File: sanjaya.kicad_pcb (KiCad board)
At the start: 2 copper layers, 72 parts, among them J1 PWR_SUPPLY, J10 Battery_Backup_Bypass, J11 USB_B_Micro_OUT, J12 ON_Switch, J13 Raspberry_Pi_2_3, J14 Fan, J15 Serial, J2 Digital_Input_Signals, J3 Digital_Gnd, J4 Screw_Terminal_01x03, J5 Screw_Terminal_01x03, J6 Screw_Terminal_01x02, J7 Screw_Terminal_01x02, J8 Supply_Safety_Bypass, J9 USB_B_Micro_IN, K1 Songle-SRD, K2 Songle-SRD, Q1 Q_PMOS_GSD, Q2 FDC021N30, SW2 SW_DIP_x04, U1 74HC14, U2 MCP9700T-ETT, U3 TPS2400BVR, U4 ULN2803A, U5 MCP3428, U6 TLP291-4, U7 MAX232, U8 SN65LBC176D

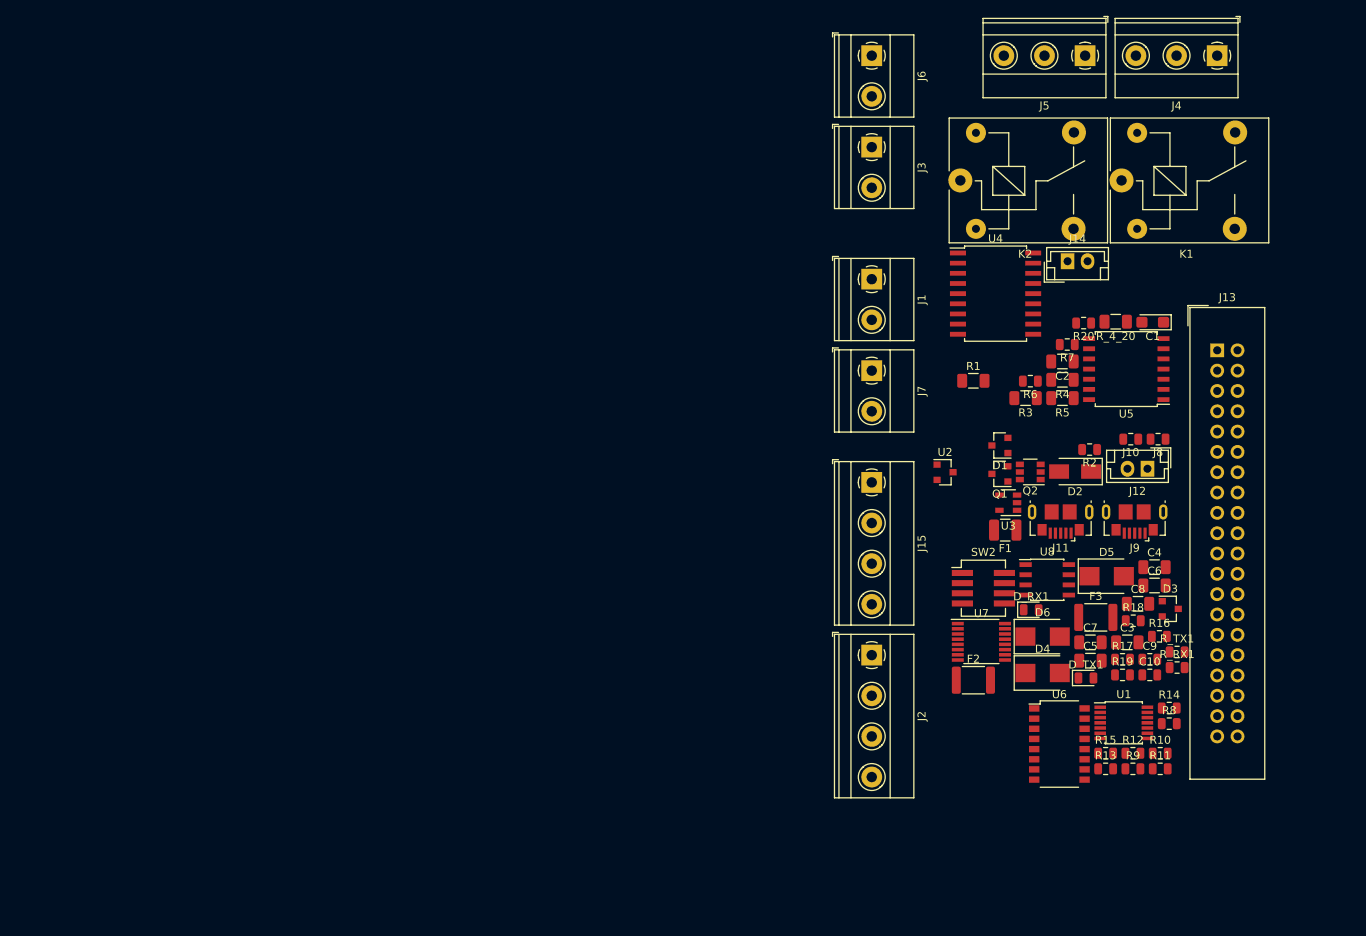
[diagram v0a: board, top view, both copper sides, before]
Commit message: Changes: 1. Removed TVS diodes in favour of a RS485 transceiver of the same footprint that contains ESD protection 2. Tried different layouts.
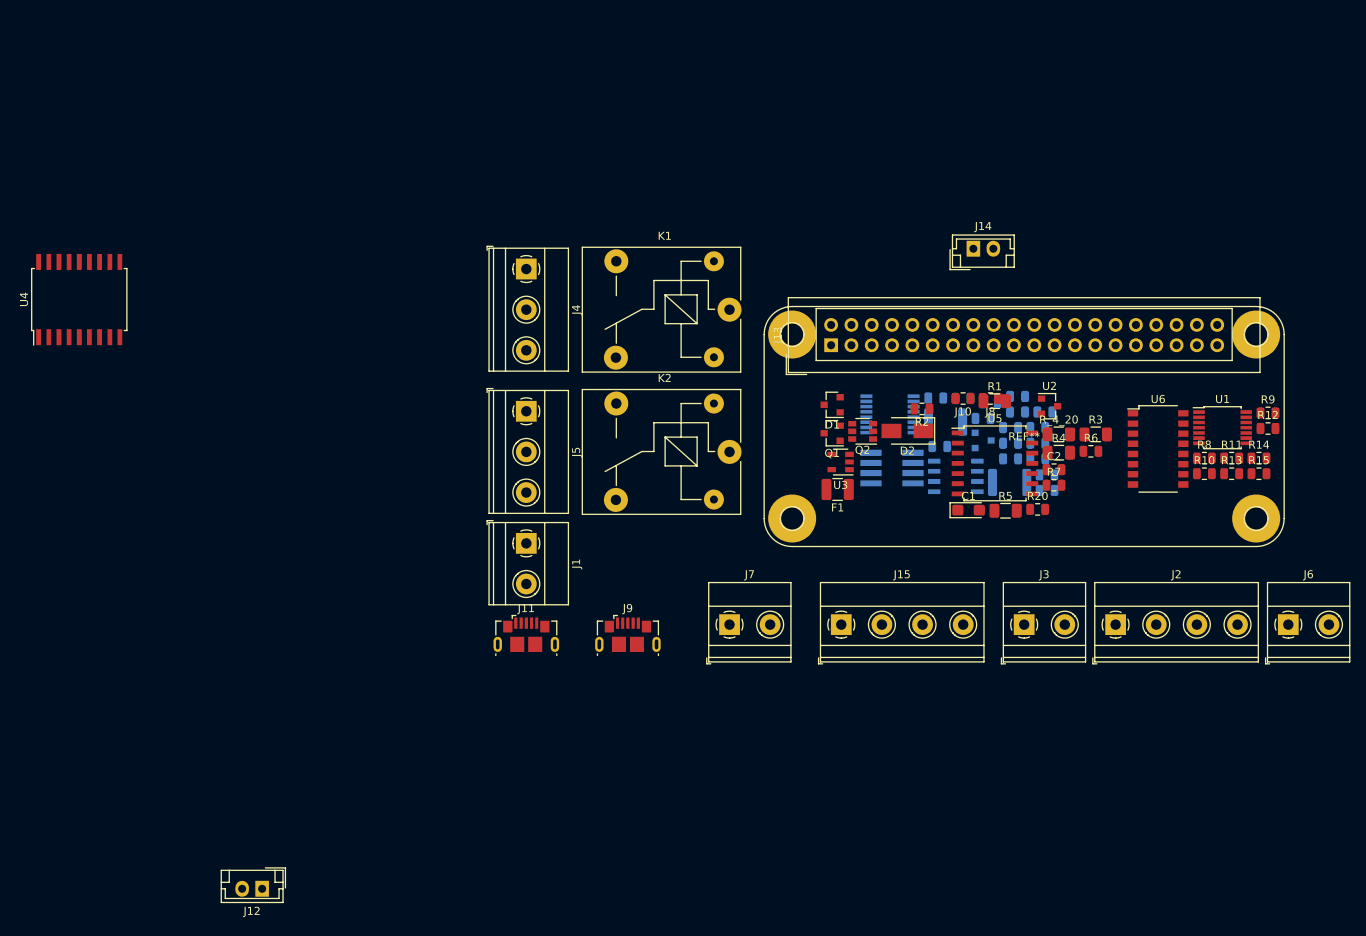
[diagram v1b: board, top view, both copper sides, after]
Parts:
- removed D4, D5, D6: TVS, Diode_SMD:D_SMB
- added REF**: RaspberryPI_ZeroW, Custom Boards:RaspberryPI_ZeroW, F.Cu at (141.0, 99.7)
- C10, C9, D3, D_RX1, D_TX1, F2, F3, R16, R17, R18, R19, R_RX1, R_TX1, SW2, U7: moved to B.Cu
- C2: footprint Capacitor_SMD:C_1206_3216Metric -> Capacitor_SMD:C_0805_2012Metric
- C3, C4, C5, C6, C7, C8: footprint Capacitor_SMD:C_1206_3216Metric -> Capacitor_SMD:C_0805_2012Metric; moved to B.Cu
- U8: value SN65LBC176D -> SN65HVD75DR; moved to B.Cu
- moved J12 122.5 mm to (45.7, 157.5)
- moved U4 114.5 mm to (22.9, 83.8), turned to 90 degrees
- moved J4 90.4 mm to (78.7, 80.0), turned to 270 degrees
- moved J6 88.1 mm to (174.0, 124.5), turned to 0 degrees
- moved J5 82.8 mm to (78.7, 97.8), turned to 270 degrees
- moved J11 68.3 mm to (78.7, 125.7), turned to 0 degrees
- moved J9 64.9 mm to (91.4, 125.7), turned to 0 degrees
- moved J3 62.7 mm to (141.0, 124.5), turned to 0 degrees
- moved J1 54.4 mm to (78.7, 114.3)
- moved K1 51.6 mm to (104.1, 85.1), turned to 180 degrees
- moved J13 48.3 mm to (116.8, 89.5), turned to 90 degrees
- moved R9 47.6 mm to (171.5, 98.0)
- moved K2 44.5 mm to (104.1, 102.9), turned to 180 degrees
- moved R12 44.0 mm to (171.5, 99.9)
- moved R13 40.1 mm to (166.9, 105.6)
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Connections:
- D3 pad 1: Net-(C4-Pad1) -> Net-(D3-Pad1)
- D3 pad 2: (no net) -> Net-(C4-Pad1)
- J11 pad 2: Net-(J11-Pad2) -> (no net)
- J11 pad 3: Net-(J11-Pad3) -> (no net)
- J11 pad 4: Net-(J11-Pad4) -> (no net)
- J13 pad 11: Net-(J13-Pad11) -> (no net)
- J13 pad 12: Net-(J13-Pad12) -> (no net)
- J13 pad 13: Net-(J13-Pad13) -> (no net)
- J13 pad 17: Net-(J13-Pad17) -> (no net)
- J13 pad 19: Net-(J13-Pad19) -> (no net)
- J13 pad 21: Net-(J13-Pad21) -> (no net)
- J13 pad 23: Net-(J13-Pad23) -> (no net)
- J13 pad 24: Net-(J13-Pad24) -> (no net)
- J13 pad 26: Net-(J13-Pad26) -> (no net)
- J13 pad 27: Net-(J13-Pad27) -> (no net)
- J13 pad 28: Net-(J13-Pad28) -> (no net)
- J13 pad 32: Net-(J13-Pad32) -> (no net)
- J13 pad 33: Net-(J13-Pad33) -> (no net)
- J13 pad 35: Net-(J13-Pad35) -> (no net)
- J13 pad 36: Net-(J13-Pad36) -> (no net)
- J13 pad 37: Net-(J13-Pad37) -> (no net)
- J13 pad 38: Net-(J13-Pad38) -> (no net)
- J13 pad 40: Net-(J13-Pad40) -> (no net)
- J9 pad 2: Net-(J9-Pad2) -> (no net)
- J9 pad 3: Net-(J9-Pad3) -> (no net)
- J9 pad 4: Net-(J9-Pad4) -> (no net)
- R16 pad 1: Net-(D3-Pad3) -> Net-(D3-Pad1)
- SW2 pad 5: Net-(D3-Pad3) -> Net-(D3-Pad1)
- U3 pad 1: Net-(U3-Pad1) -> (no net)
- U3 pad 3: Net-(U3-Pad3) -> (no net)
- U7 pad 10: Net-(U7-Pad10) -> (no net)
- U7 pad 7: Net-(U7-Pad7) -> (no net)
- U7 pad 8: Net-(U7-Pad8) -> (no net)
- U7 pad 9: Net-(U7-Pad9) -> (no net)
- U8 pad 1: Net-(D3-Pad3) -> Net-(D3-Pad1)

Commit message: Changes: 1. Some net names, connector names changed to be more meaningful 2. I2C connector added 3. Mistake in power bank bypass connection rectified 4. Layout changed. Almost finalized.
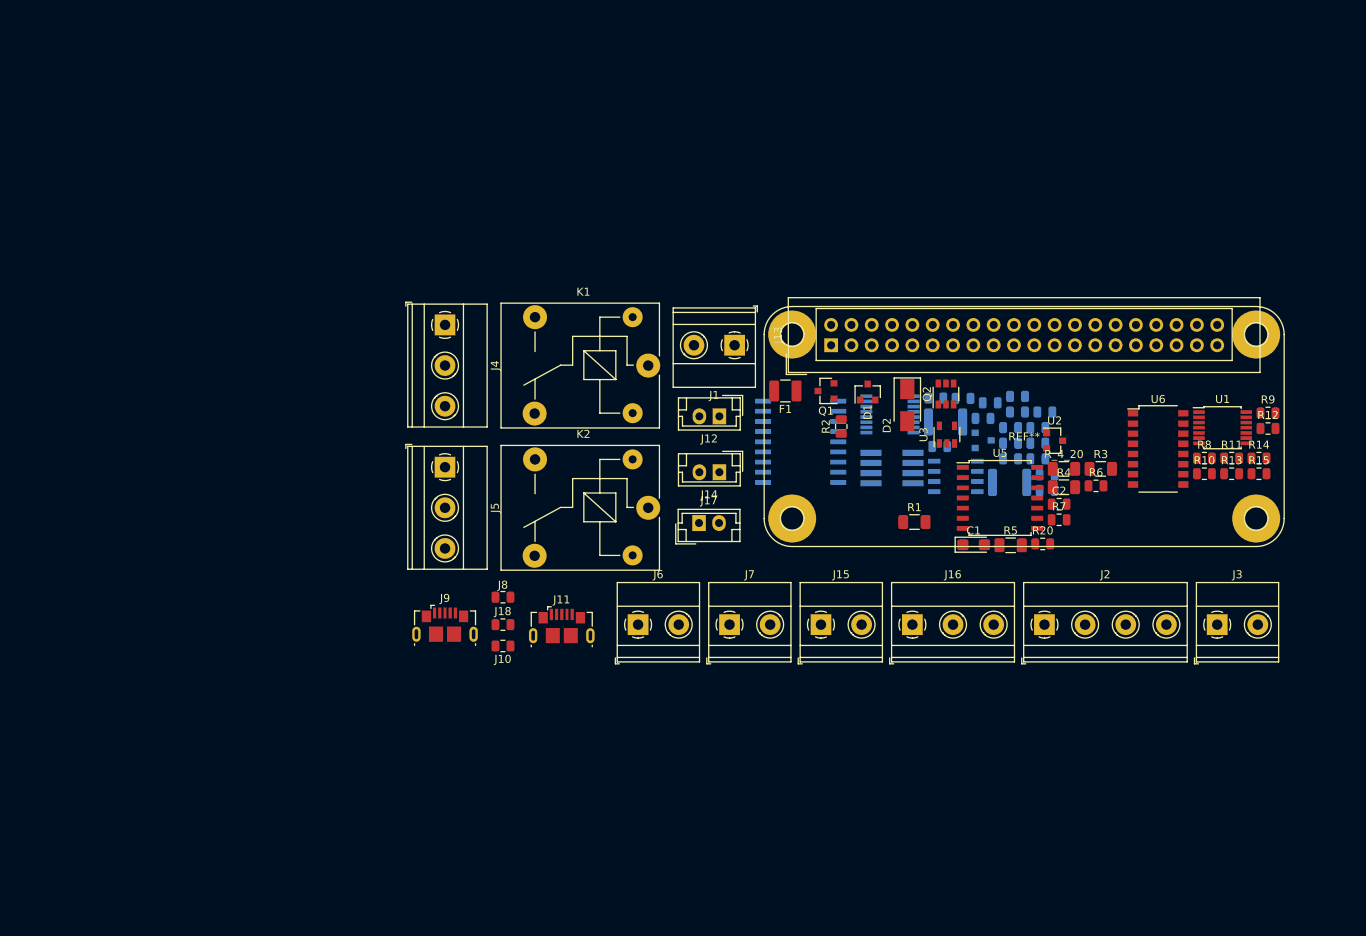
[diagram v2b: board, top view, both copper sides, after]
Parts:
- added J16: RS485, TerminalBlock_Phoenix:TerminalBlock_Phoenix_MKDS-1,5-3-5.08_1x03_P5.08mm_Horizontal, F.Cu at (127.0, 124.5)
- added J17: I2C, Connector_JST:JST_EH_B02B-EH-A_1x02_P2.50mm_Vertical, F.Cu at (100.3, 111.8)
- added J18: Bat_Bak_Byp_Vcc, Resistor_SMD:R_0805_2012Metric, F.Cu at (75.8, 124.5)
- J10: value Battery_Backup_Bypass -> Bat_Bak_Byp_Gnd
- J15: value Serial -> RS232; footprint TerminalBlock_Phoenix:TerminalBlock_Phoenix_MKDS-1,5-4-5.08_1x04_P5.08mm_Horizontal -> TerminalBlock_Phoenix:TerminalBlock_Phoenix_MKDS-1,5-2-5.08_1x02_P5.08mm_Horizontal
- J3: value Digital_Gnd -> Digital_Input_Gnd
- J6: value Screw_Terminal_01x02 -> Analog_RSense
- J7: value Screw_Terminal_01x02 -> Analog_420
- U4: moved to B.Cu
- moved U4 91.9 mm to (113.0, 101.6), turned to 0 degrees
- moved J12 82.2 mm to (102.9, 98.4)
- moved J6 81.3 mm to (92.7, 124.5)
- moved J8 65.8 mm to (75.8, 121.0)
- moved J10 65.3 mm to (75.8, 127.1)
- moved J14 42.3 mm to (102.9, 105.4), turned to 180 degrees
- moved J1 35.9 mm to (104.8, 89.5), turned to 180 degrees
- moved J3 24.1 mm to (165.1, 124.5)
- moved J9 22.9 mm to (68.6, 124.5)
- moved R1 18.1 mm to (127.3, 111.6)
- moved F1 13.9 mm to (111.1, 95.2)
- moved U3 13.7 mm to (131.3, 100.7), turned to 90 degrees
- moved J4 12.3 mm to (68.6, 87.0)
- moved J5 12.3 mm to (68.6, 104.8)
- moved K1 12.3 mm to (94.0, 92.1)
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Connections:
- net /I_Sense+ renamed /3V3_Net+
- J15 pad 1: /serial/RS485_B- -> /serial/RS232_RX
- J15 pad 2: /serial/RS485_A+ -> /serial/RS232_TX
- J4 pad 1: /actuation/RL1_NC -> /actuation/RL1_NO
- J4 pad 3: /actuation/RL1_NO -> /actuation/RL1_NC
- J5 pad 1: /actuation/RL2_NC -> /actuation/RL2_NO
- J5 pad 3: /actuation/RL2_NO -> /actuation/RL2_NC

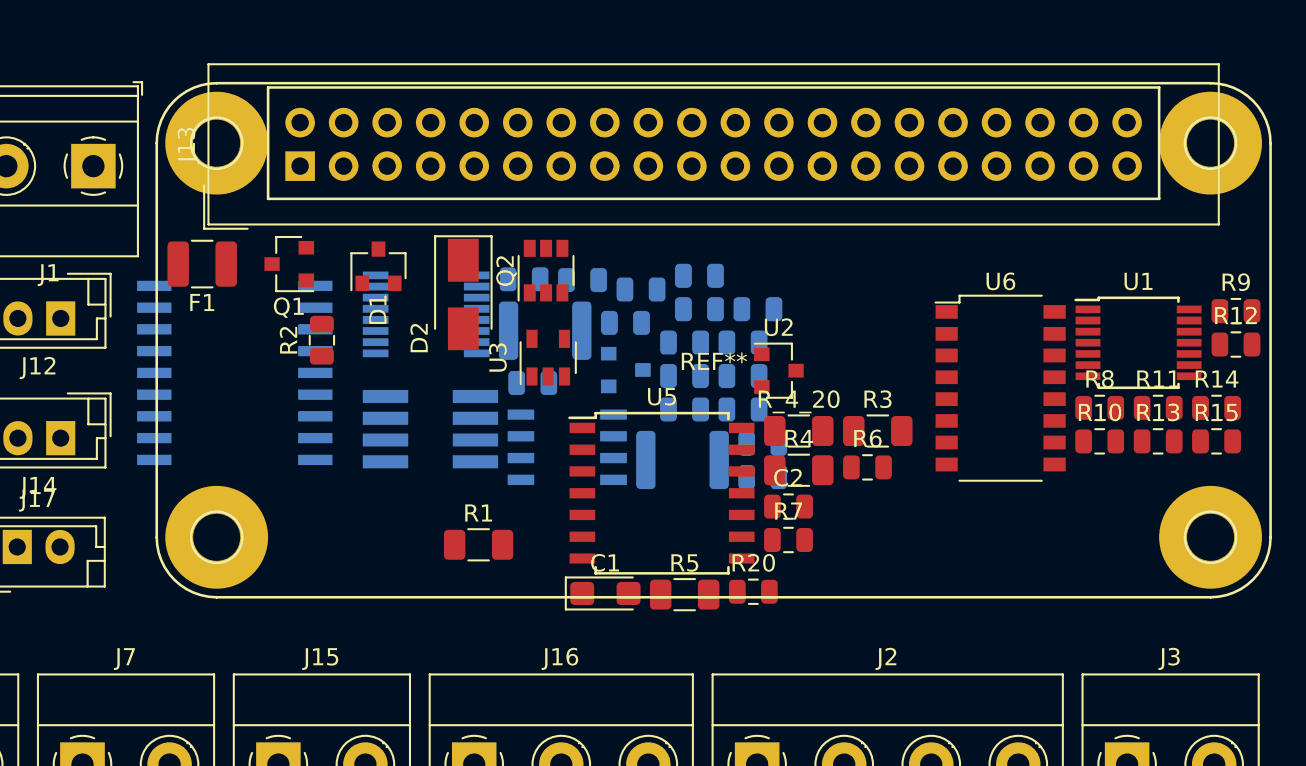
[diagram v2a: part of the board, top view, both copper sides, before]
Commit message: Changes: 1. Laid out the ADC part 2. Removed an unnecessary 10K resistor in the ADC voltage sense part
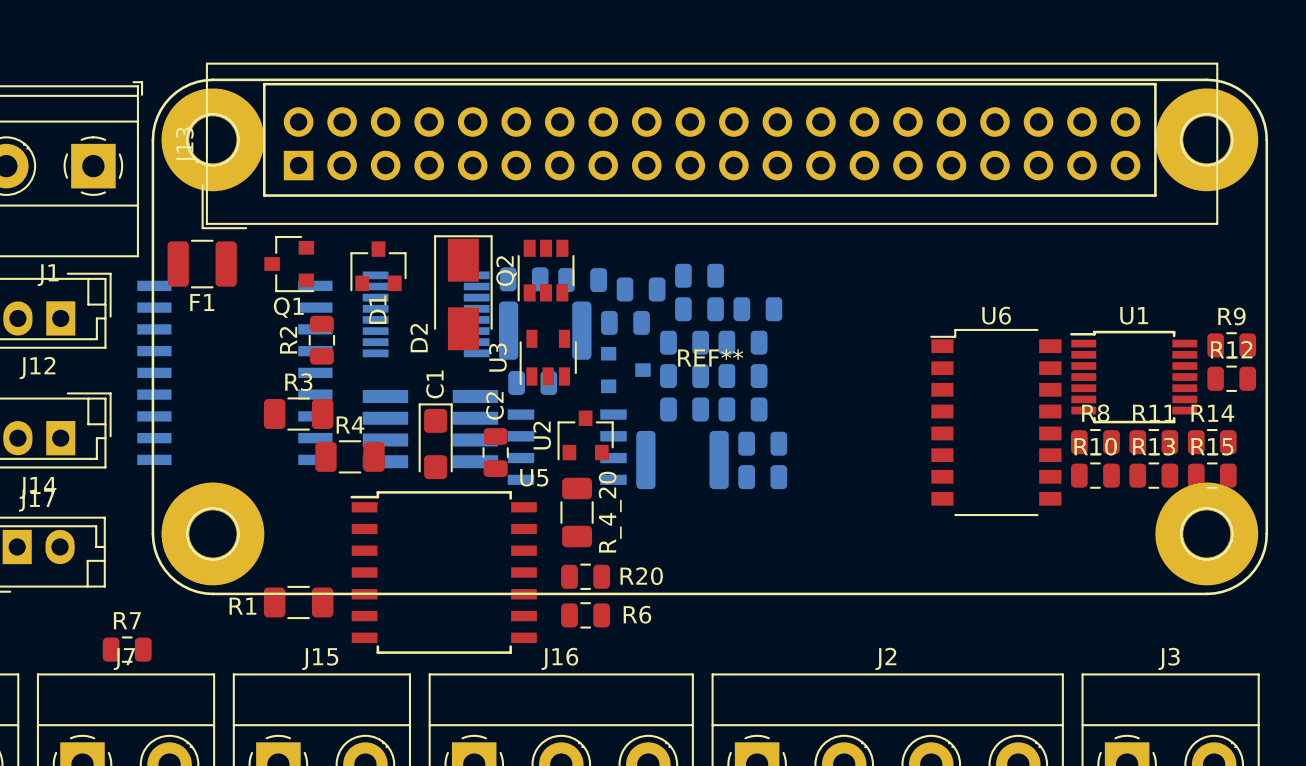
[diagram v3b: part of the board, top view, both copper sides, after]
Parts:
- removed R5: 10K, Resistor_SMD:R_1206_3216Metric
- moved R7 39.1 mm to (106.8, 117.8)
- moved R3 33.8 mm to (116.8, 104.0)
- moved R4 26.2 mm to (119.8, 106.5)
- moved R6 18.6 mm to (133.5, 115.8)
- moved C2 17.4 mm to (128.2, 106.2), turned to 270 degrees
- moved R_4_20 13.8 mm to (133.0, 109.8), turned to 270 degrees
- moved U5 13.5 mm to (125.2, 113.2)
- moved C1 13.2 mm to (124.8, 105.8), turned to 270 degrees
- moved U2 11.9 mm to (133.5, 105.2), turned to 90 degrees
- moved R1 11.0 mm to (116.8, 115.0)
- moved R20 9.83 mm to (133.5, 113.5)
- moved R10 2.02 mm to (163.3, 107.6)
- moved R11 2.02 mm to (166.7, 105.6)
- moved R12 2.02 mm to (171.2, 101.9)
- moved R13 2.02 mm to (166.7, 107.6)
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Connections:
- R4 pad 2: Net-(R4-Pad2) -> /AGND
